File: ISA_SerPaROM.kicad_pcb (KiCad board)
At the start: 2 copper layers, 158.8 x 102.9 mm, 77 parts, among them J1 ISA BUS, J10 Parallel Port, J11 Serial 4 IDC, J12 Serial 3 IDC, J13 UART4_SEL, J2 ADDR_IRQ, J3 UART1_SEL, J4 UART2_SEL, J5 ADDR, J6 Serial 2 IDC, J7 Serial 1 DB9, J8 UART3_SEL, J9 Parport IRQ Select, U1 74HCT138, U11 74LS30, U12 74LS86, U13 74LS02, U14 74LS155, U15 74LS245, U16 74LS174, U17 74LS374, U18 74LS05, U19 74LS125, U2 74HCT138, U20 74LS240, U21 74LS244, U23 16C554, U24 74HCT32, U25 GD75232N, U26 GD75232N, U29 74HCT245, U30 74HCT21, U5 GD75232N, U6 GD75232N, X1 1.8432Mhz

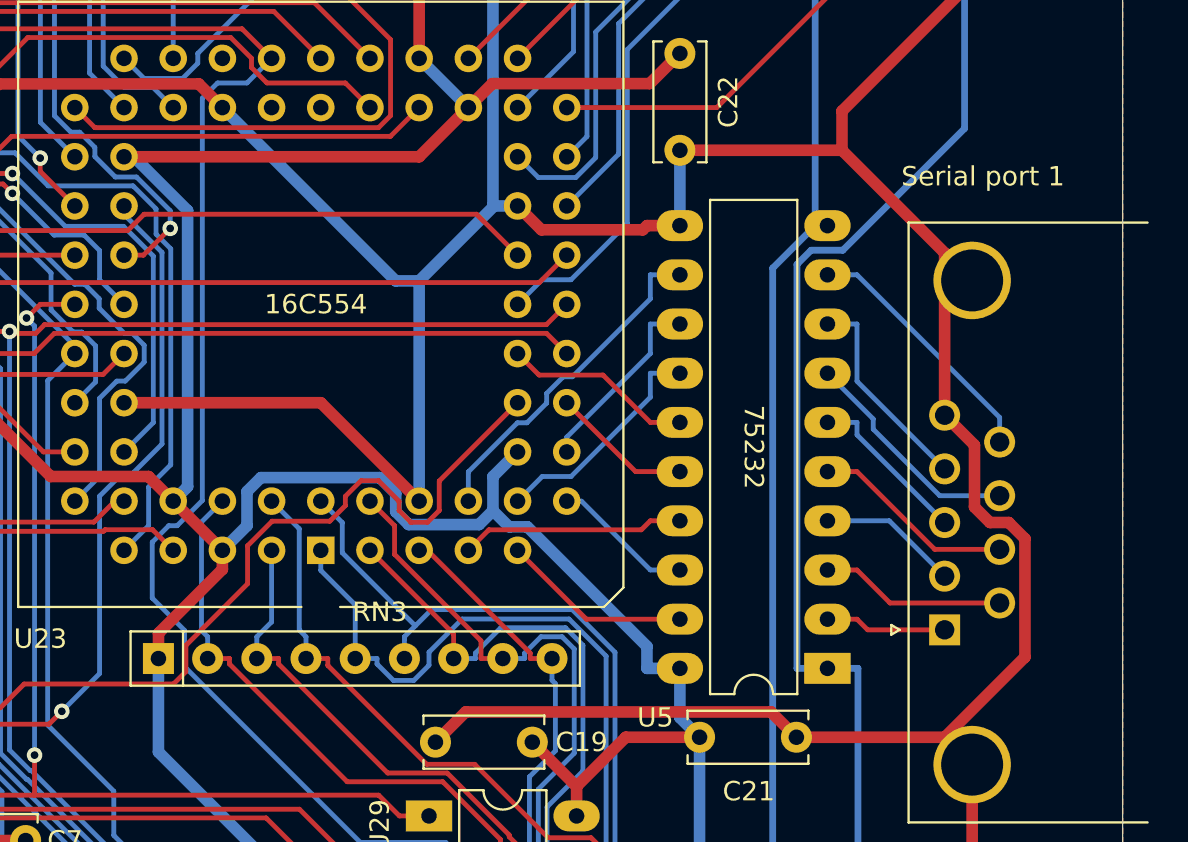
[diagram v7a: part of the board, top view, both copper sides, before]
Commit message: Slightly adjust the silkscreen
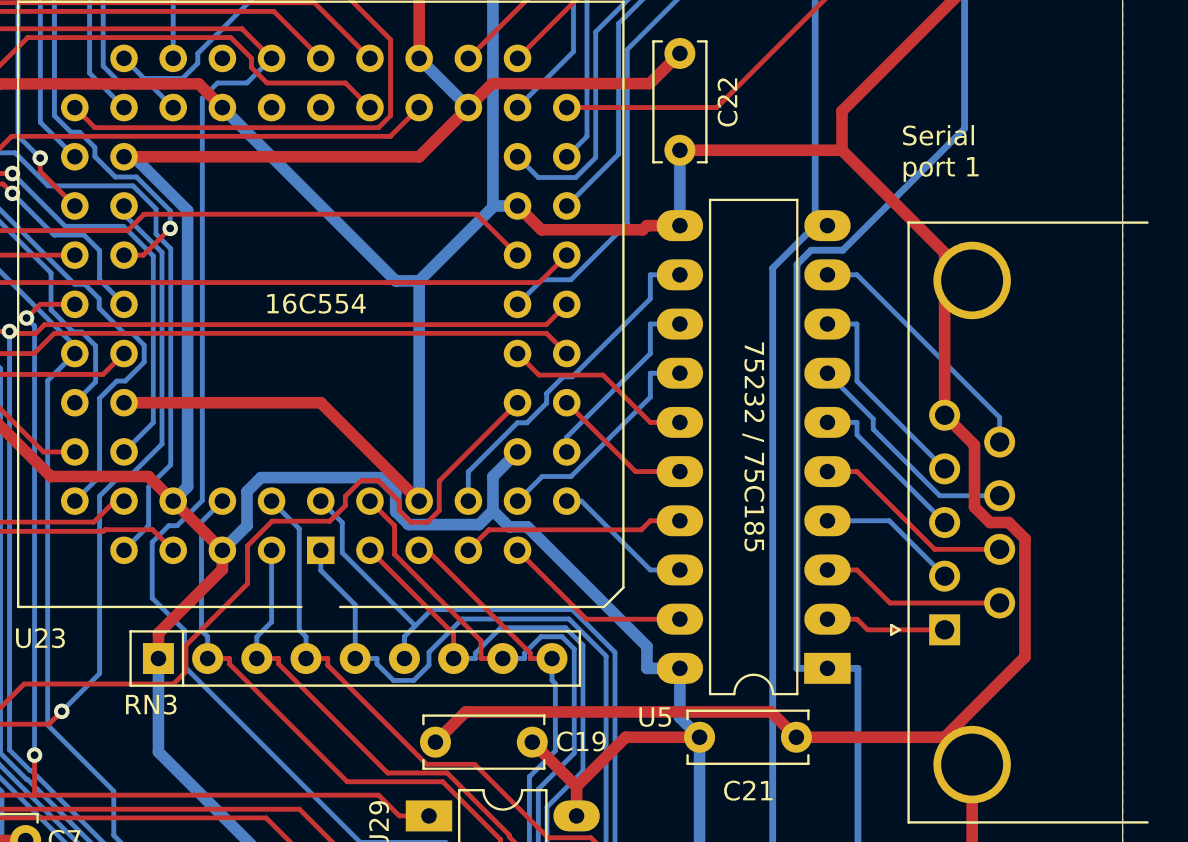
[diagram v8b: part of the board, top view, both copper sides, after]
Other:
- board text removed: "75232"
